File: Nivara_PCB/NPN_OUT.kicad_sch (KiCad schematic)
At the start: 16 parts, among them Q1 AO3407A, Q2 AO3407A, U8 LTV-357T, U9 LTV-357T

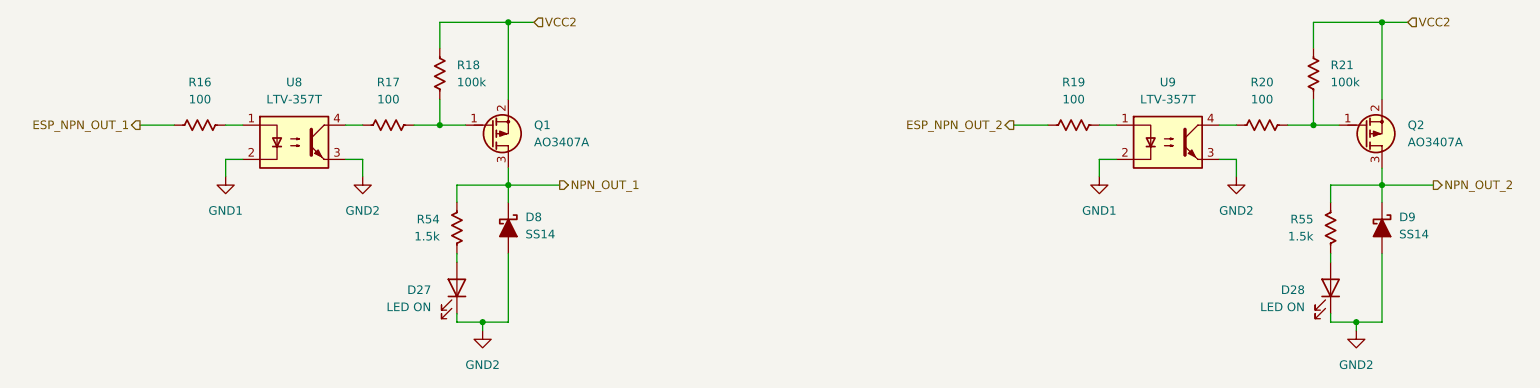
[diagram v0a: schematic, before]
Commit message: Cambios en el PCB de Nivara. Ruteo de emtradas y salidas NPN y PNP.
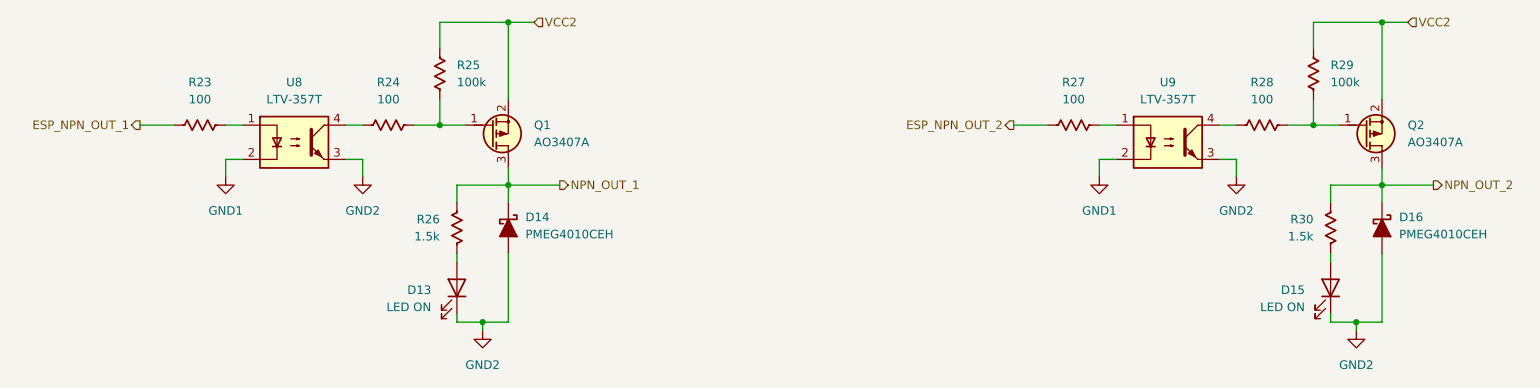
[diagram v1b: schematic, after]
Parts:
- removed D8, D9: SS14, PCM_Diode_SMD_AKL:D_SMA, symbol PCM_Diode_Schottky_AKL:SS14
- added D14, D16: PMEG4010CEH, PCM_Diode_SMD_AKL:D_SOD-123F, symbol PCM_Diode_Schottky_AKL:PMEG4010CEH
- renumbered D27 to D13, D28 to D15, R16 to R23, R17 to R24, R18 to R25, R54 to R26, R19 to R27, R20 to R28, R21 to R29, R55 to R30
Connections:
- net GND2: now also D14.2 (A), D16.2 (A)
- net NPN_OUT_1: now also D14.1 (K)
- net NPN_OUT_2: now also D16.1 (K)
